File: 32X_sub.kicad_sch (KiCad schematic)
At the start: 98 parts, among them IC511 315-5684, IC512 315-5788, IC515 74HC74, IC516 74LS00, T520 TestPoint, T526 TestPoint, T527 TestPoint, T528 TestPoint, T547 TestPoint, T548 TestPoint, T555 TestPoint, T599 AS, X501 *3

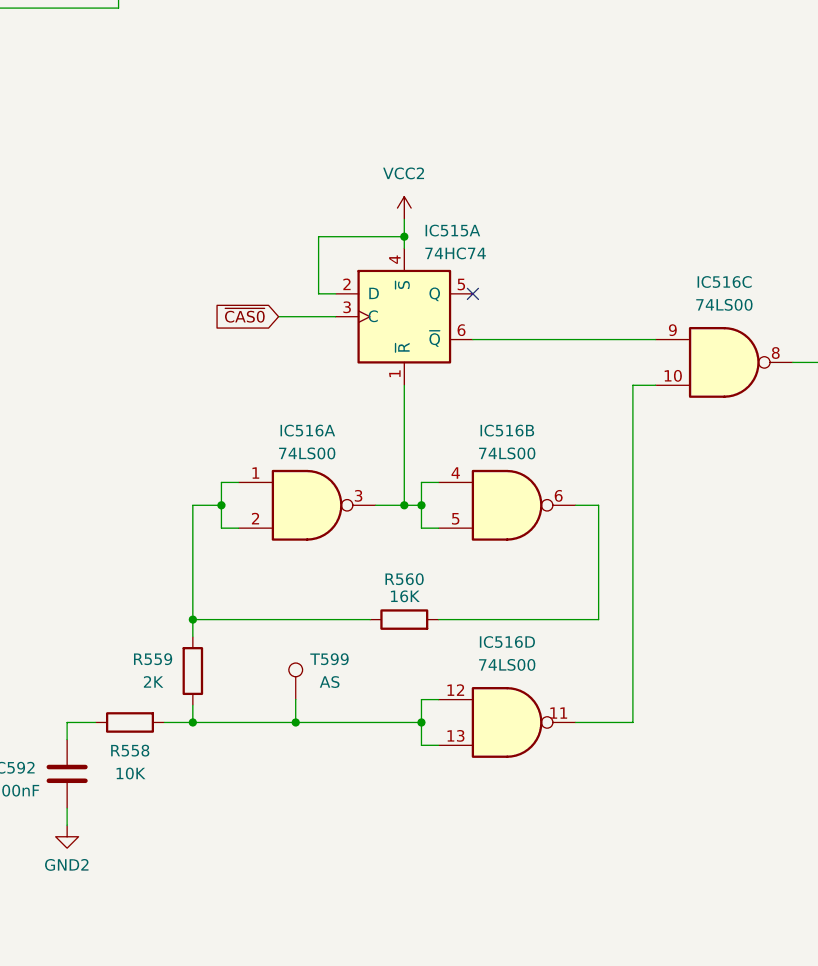
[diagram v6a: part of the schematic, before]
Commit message: Review/add 32X bodges.
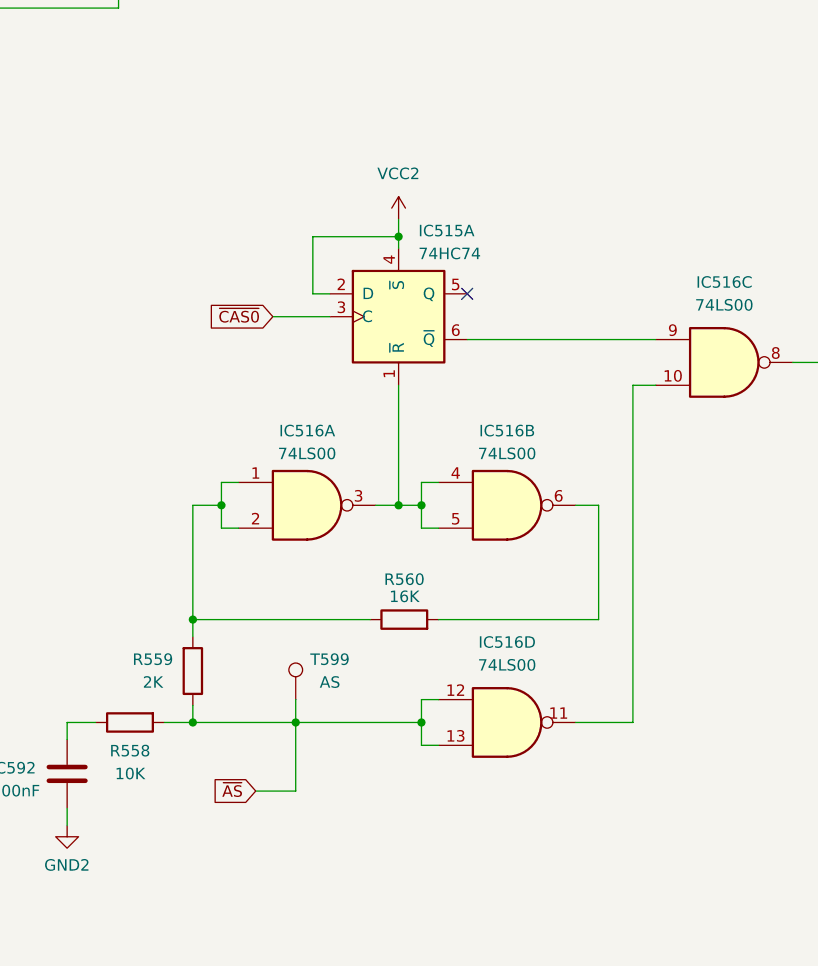
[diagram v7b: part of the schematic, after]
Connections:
- net ~{AS}: now reaches IC516.12, IC516.13, R558.2, R559.1, T599.1
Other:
- moved on the sheet: IC515A
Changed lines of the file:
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@@
   (junction (at 172.085 254.635) (diameter 0) (color 0 0 0 0)
   )
+  (junction (at 183.515 230.505) (diameter 0) (color 0 0 0 0)
+  )
   (junction (at 97.155 129.54) (diameter 0) (color 0 0 0 0)
   )
-  (junction (at 184.15 200.66) (diameter 0) (color 0 0 0 0)
+  (junction (at 183.515 200.66) (diameter 0) (color 0 0 0 0)
   )
   (junction (at 169.545 101.6) (diameter 0) (color 0 0 0 0)
@@
   (junction (at 259.08 116.84) (diameter 0) (color 0 0 0 0)
   )
-  (junction (at 184.15 230.505) (diameter 0) (color 0 0 0 0)
-  )
   (junction (at 91.44 53.34) (diameter 0) (color 0 0 0 0)
   )
@@
   (no_connect (at 134.62 86.36))
   (no_connect (at 134.62 93.98))
-  (no_connect (at 191.77 207.01))
+  (no_connect (at 191.135 207.01))
   (no_connect (at 134.62 88.9))
   (no_connect (at 134.62 91.44))
@@
     (stroke (width 0) (type default))
   )
-  (wire (pts (xy 174.625 207.01) (xy 174.625 200.66))
+  (wire (pts (xy 173.99 207.01) (xy 173.99 200.66))
     (stroke (width 0) (type default))
   )
@@
     (stroke (width 0) (type default))
   )
-  (wire (pts (xy 184.15 230.505) (xy 184.15 217.17))
+  (wire (pts (xy 183.515 230.505) (xy 183.515 217.17))
     (stroke (width 0) (type default))
   )
@@
     (stroke (width 0) (type default))
   )
-  (wire (pts (xy 176.53 207.01) (xy 174.625 207.01))
+  (wire (pts (xy 175.895 207.01) (xy 173.99 207.01))
     (stroke (width 0) (type default))
   )
@@
     (stroke (width 0) (type default))
   )
-  (wire (pts (xy 184.15 198.755) (xy 184.15 200.66))
+  (wire (pts (xy 183.515 198.755) (xy 183.515 200.66))
     (stroke (width 0) (type default))
   )
@@
     (stroke (width 0) (type default))
   )
-  (wire (pts (xy 180.975 230.505) (xy 184.15 230.505))
+  (wire (pts (xy 180.975 230.505) (xy 183.515 230.505))
+    (stroke (width 0) (type default))
+  )
+  (wire (pts (xy 172.085 262.255) (xy 172.085 254.635))
     (stroke (width 0) (type default))
   )
@@
     (stroke (width 0) (type default))
   )
-  (wire (pts (xy 184.15 230.505) (xy 186.055 230.505))
-    (stroke (width 0) (type default))
-  )
   (wire (pts (xy 270.51 38.1) (xy 270.51 44.45))
     (stroke (width 0) (type default))
@@
     (stroke (width 0) (type default))
   )
+  (wire (pts (xy 167.64 262.255) (xy 172.085 262.255))
+    (stroke (width 0) (type default))
+  )
   (wire (pts (xy 240.665 38.1) (xy 252.73 38.1))
     (stroke (width 0) (type default))
@@
     (stroke (width 0) (type default))
   )
+  (wire (pts (xy 183.515 230.505) (xy 186.055 230.505))
+    (stroke (width 0) (type default))
+  )
   (wire (pts (xy 326.39 88.9) (xy 330.835 88.9))
     (stroke (width 0) (type default))
@@
     (stroke (width 0) (type default))
   )
-  (wire (pts (xy 184.15 200.66) (xy 184.15 201.93))
+  (wire (pts (xy 183.515 200.66) (xy 183.515 201.93))
     (stroke (width 0) (type default))
   )
@@
     (stroke (width 0) (type default))
   )
-  (wire (pts (xy 170.18 209.55) (xy 176.53 209.55))
+  (wire (pts (xy 169.545 209.55) (xy 175.895 209.55))
     (stroke (width 0) (type default))
   )
@@
     (stroke (width 0) (type default))
   )
-  (wire (pts (xy 174.625 200.66) (xy 184.15 200.66))
+  (wire (pts (xy 173.99 200.66) (xy 183.515 200.66))
     (stroke (width 0) (type default))
   )
@@
     (stroke (width 0) (type default))
   )
-  (wire (pts (xy 191.77 212.09) (xy 212.09 212.09))
+  (wire (pts (xy 191.135 212.09) (xy 212.09 212.09))
     (stroke (width 0) (type default))
   )
@@
     )
   )
+  (global_label "~{AS}" (shape input) (at 167.64 262.255 180) (fields_autoplaced)
+    (effects (font (size 1.27 1.27)) (justify right))
+    (property "Intersheetrefs" "${INTERSHEET_REFS}" (at 162.3567 262.255 0)
+      (effects (font (size 1.27 1.27)) (justify right) hide)
+    )
+  )
   (global_label "XBOUT" (shape output) (at 367.665 43.18 0) (fields_autoplaced)
     (effects (font (size 1.27 1.27)) (justify left))
@@
     )
   )
-  (global_label "~{CAS0}" (shape input) (at 170.18 209.55 180) (fields_autoplaced)
+  (global_label "~{CAS0}" (shape input) (at 169.545 209.55 180) (fields_autoplaced)
     (effects (font (size 1.27 1.27)) (justify right))
-    (property "Intersheetrefs" "${INTERSHEET_REFS}" (at 162.4172 209.55 0)
+    (property "Intersheetrefs" "${INTERSHEET_REFS}" (at 161.7822 209.55 0)
       (effects (font (size 1.27 1.27)) (justify right) hide)
     )
@@
     )
   )
-  (symbol (lib_id "74xx:74LS74") (at 184.15 209.55 0) (unit 1)
+  (symbol (lib_id "74xx:74LS74") (at 183.515 209.55 0) (unit 1)
     (in_bom yes) (on_board yes) (dnp no) (fields_autoplaced)
-    (property "Reference" "IC515" (at 186.3441 200.025 0)
+    (property "Reference" "IC515" (at 185.7091 200.025 0)
       (effects (font (size 1.27 1.27)) (justify left))
     )
-    (property "Value" "74HC74" (at 186.3441 202.565 0)
+    (property "Value" "74HC74" (at 185.7091 202.565 0)
       (effects (font (size 1.27 1.27)) (justify left))
     )
-    (property "Footprint" "Package_SO:SO-14_3.9x8.65mm_P1.27mm" (at 184.15 209.55 0)
+    (property "Footprint" "Package_SO:SO-14_3.9x8.65mm_P1.27mm" (at 183.515 209.55 0)
       (effects (font (size 1.27 1.27)) hide)
     )
-    (property "Datasheet" "74xx/74hc_hct74.pdf" (at 184.15 209.55 0)
+    (property "Datasheet" "74xx/74hc_hct74.pdf" (at 183.515 209.55 0)
       (effects (font (size 1.27 1.27)) hide)
     )
@@
     )
   )
-  (symbol (lib_id "32X:VCC2") (at 184.15 198.755 0) (unit 1)
+  (symbol (lib_id "32X:VCC2") (at 183.515 198.755 0) (unit 1)
     (in_bom yes) (on_board yes) (dnp no) (fields_autoplaced)
-    (property "Reference" "#PWR0137" (at 184.15 202.565 0)
+    (property "Reference" "#PWR0137" (at 183.515 202.565 0)
       (effects (font (size 1.27 1.27)) hide)
     )
-    (property "Value" "VCC2" (at 184.15 193.675 0)
+    (property "Value" "VCC2" (at 183.515 193.675 0)
       (effects (font (size 1.27 1.27)))
     )
-    (property "Footprint" "" (at 184.15 198.755 0)
+    (property "Footprint" "" (at 183.515 198.755 0)
       (effects (font (size 1.27 1.27)) hide)
     )
-    (property "Datasheet" "" (at 184.15 198.755 0)
+    (property "Datasheet" "" (at 183.515 198.755 0)
       (effects (font (size 1.27 1.27)) hide)
     )

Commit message: Schematic review/fixes.
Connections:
- net VCC2: now also C592.2, R558.1
- net at IC511.30 (HPIN2), R517.1, R518.2: no longer R519.2
- net at C557.1, IC511.6 (MOUT1): now also R519.2
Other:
- moved on the sheet: R519, R520
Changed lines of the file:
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@@
   (junction (at 112.395 250.19) (diameter 0) (color 0 0 0 0)
   )
-  (junction (at 91.44 114.3) (diameter 0) (color 0 0 0 0)
-  )
   (junction (at 270.51 66.04) (diameter 0) (color 0 0 0 0)
   )
   (junction (at 142.875 149.86) (diameter 0) (color 0 0 0 0)
   )
-  (junction (at 97.155 147.32) (diameter 0) (color 0 0 0 0)
-  )
   (junction (at 91.44 47.625) (diameter 0) (color 0 0 0 0)
   )
@@
   (junction (at 328.93 129.54) (diameter 0) (color 0 0 0 0)
   )
+  (junction (at 146.685 254.635) (diameter 0) (color 0 0 0 0)
+  )
   (junction (at 112.395 219.71) (diameter 0) (color 0 0 0 0)
   )
@@
   (junction (at 260.35 71.12) (diameter 0) (color 0 0 0 0)
   )
+  (junction (at 91.44 124.46) (diameter 0) (color 0 0 0 0)
+  )
   (junction (at 328.93 142.24) (diameter 0) (color 0 0 0 0)
   )
@@
   (junction (at 183.515 230.505) (diameter 0) (color 0 0 0 0)
   )
-  (junction (at 97.155 129.54) (diameter 0) (color 0 0 0 0)
-  )
   (junction (at 183.515 200.66) (diameter 0) (color 0 0 0 0)
   )
@@
   (junction (at 186.055 230.505) (diameter 0) (color 0 0 0 0)
   )
-  (junction (at 97.155 138.43) (diameter 0) (color 0 0 0 0)
+  (junction (at 91.44 138.43) (diameter 0) (color 0 0 0 0)
   )
   (junction (at 160.655 243.205) (diameter 0) (color 0 0 0 0)
@@
   (junction (at 252.73 38.1) (diameter 0) (color 0 0 0 0)
   )
+  (junction (at 91.44 147.32) (diameter 0) (color 0 0 0 0)
+  )
   (junction (at 160.655 254.635) (diameter 0) (color 0 0 0 0)
   )
@@
   (junction (at 351.79 99.06) (diameter 0) (color 0 0 0 0)
   )
+  (junction (at 83.82 114.3) (diameter 0) (color 0 0 0 0)
+  )
   (no_connect (at 295.91 116.84))
   (no_connect (at 332.74 226.695))
@@
     (stroke (width 0) (type default))
   )
-  (wire (pts (xy 97.155 138.43) (xy 97.155 139.065))
+  (wire (pts (xy 91.44 138.43) (xy 91.44 139.065))
     (stroke (width 0) (type default))
   )
@@
     (stroke (width 0) (type default))
   )
-  (wire (pts (xy 97.155 147.32) (xy 83.82 147.32))
-    (stroke (width 0) (type default))
-  )
   (wire (pts (xy 53.975 73.66) (xy 64.135 73.66))
     (stroke (width 0) (type default))
@@
     (stroke (width 0) (type default))
   )
-  (wire (pts (xy 83.82 114.3) (xy 91.44 114.3))
-    (stroke (width 0) (type default))
-  )
   (wire (pts (xy 350.52 127) (xy 350.52 128.27))
     (stroke (width 0) (type default))
@@
     (stroke (width 0) (type default))
   )
-  (wire (pts (xy 97.155 138.43) (xy 104.14 138.43))
+  (wire (pts (xy 91.44 138.43) (xy 104.14 138.43))
     (stroke (width 0) (type default))
   )
@@
     (stroke (width 0) (type default))
   )
-  (wire (pts (xy 104.14 129.54) (xy 97.155 129.54))
+  (wire (pts (xy 83.82 129.54) (xy 104.14 129.54))
     (stroke (width 0) (type default))
   )
@@
     (stroke (width 0) (type default))
   )
-  (wire (pts (xy 104.14 114.3) (xy 91.44 114.3))
+  (wire (pts (xy 83.82 114.3) (xy 104.14 114.3))
     (stroke (width 0) (type default))
   )
@@
     (stroke (width 0) (type default))
   )
-  (wire (pts (xy 97.155 129.54) (xy 97.155 130.175))
-    (stroke (width 0) (type default))
-  )
   (wire (pts (xy 152.4 33.02) (xy 152.4 55.88))
     (stroke (width 0) (type default))
@@
     (stroke (width 0) (type default))
   )
+  (wire (pts (xy 91.44 124.46) (xy 104.14 124.46))
+    (stroke (width 0) (type default))
+  )
   (wire (pts (xy 196.215 33.02) (xy 202.565 33.02))
     (stroke (width 0) (type default))
@@
     (stroke (width 0) (type default))
   )
+  (wire (pts (xy 91.44 124.46) (xy 91.44 130.175))
+    (stroke (width 0) (type default))
+  )
   (wire (pts (xy 240.665 71.12) (xy 248.92 71.12))
     (stroke (width 0) (type default))
@@
     (stroke (width 0) (type default))
   )
-  (wire (pts (xy 91.44 109.22) (xy 93.345 109.22))
+  (wire (pts (xy 83.82 109.22) (xy 93.345 109.22))
+    (stroke (width 0) (type default))
+  )
+  (wire (pts (xy 146.685 251.46) (xy 146.685 254.635))
     (stroke (width 0) (type default))
   )
@@
     (stroke (width 0) (type default))
   )
+  (wire (pts (xy 91.44 147.32) (xy 83.82 147.32))
+    (stroke (width 0) (type default))
+  )
   (wire (pts (xy 340.995 127) (xy 347.98 127))
     (stroke (width 0) (type default))
@@
     (stroke (width 0) (type default))
   )
-  (wire (pts (xy 97.155 137.795) (xy 97.155 138.43))
+  (wire (pts (xy 91.44 137.795) (xy 91.44 138.43))
     (stroke (width 0) (type default))
   )
@@
     (stroke (width 0) (type default))
   )
-  (wire (pts (xy 97.155 129.54) (xy 83.82 129.54))
-    (stroke (width 0) (type default))
-  )
   (bus (pts (xy 85.09 255.27) (xy 85.09 252.73))
     (stroke (width 0) (type default))
@@
     (stroke (width 0) (type default))
   )
-  (wire (pts (xy 104.14 147.32) (xy 97.155 147.32))
+  (wire (pts (xy 91.44 147.32) (xy 104.14 147.32))
     (stroke (width 0) (type default))
   )
@@
     (stroke (width 0) (type default))
   )
-  (wire (pts (xy 97.155 146.685) (xy 97.155 147.32))
+  (wire (pts (xy 91.44 146.685) (xy 91.44 147.32))
     (stroke (width 0) (type default))
   )
@@
     (stroke (width 0) (type default))
   )
-  (wire (pts (xy 91.44 114.3) (xy 91.44 109.22))
-    (stroke (width 0) (type default))
-  )
-  (wire (pts (xy 104.14 124.46) (xy 91.44 124.46))
+  (wire (pts (xy 83.82 114.3) (xy 83.82 109.22))
     (stroke (width 0) (type default))
   )
@@
     )
   )
-  (symbol (lib_id "Device:R") (at 97.155 142.875 180) (unit 1)
+  (symbol (lib_id "Device:R") (at 91.44 142.875 180) (unit 1)
     (in_bom yes) (on_board yes) (dnp no)
-    (property "Reference" "R520" (at 101.6 142.24 0)
+    (property "Reference" "R520" (at 95.885 142.24 0)
       (effects (font (size 1.27 1.27)))
     )
-    (property "Value" "10K" (at 101.6 144.145 0)
+    (property "Value" "10K" (at 95.885 144.145 0)
       (effects (font (size 1.27 1.27)))
     )
-    (property "Footprint" "Resistor_SMD:R_0805_2012Metric" (at 98.933 142.875 90)
+    (property "Footprint" "Resistor_SMD:R_0805_2012Metric" (at 93.218 142.875 90)
       (effects (font (size 1.27 1.27)) hide)
     )
-    (property "Datasheet" "~" (at 97.155 142.875 0)
+    (property "Datasheet" "~" (at 91.44 142.875 0)
       (effects (font (size 1.27 1.27)) hide)
     )
@@
     )
   )
+  (symbol (lib_id "32X:VCC2") (at 146.685 251.46 0) (unit 1)
+    (in_bom yes) (on_board yes) (dnp no) (fields_autoplaced)
+    (property "Reference" "#PWR0185" (at 146.685 255.27 0)
+      (effects (font (size 1.27 1.27)) hide)
+    )
+    (property "Value" "VCC2" (at 146.685 246.38 0)
+      (effects (font (size 1.27 1.27)))
+    )
+    (property "Footprint" "" (at 146.685 251.46 0)
+      (effects (font (size 1.27 1.27)) hide)
+    )
+    (property "Datasheet" "" (at 146.685 251.46 0)
+      (effects (font (size 1.27 1.27)) hide)
+    )
+    (pin "1")
+    (instances
+      (project "Neptune"
+        (path "/bcc23b51-b742-4ae5-9dd6-d96a24058944/edde10e2-ce08-4180-9fbe-ab298dfbfa4c"
+          (reference "#PWR0185") (unit 1)
+        )
+      )
+    )
+  )
   (symbol (lib_id "Device:C_Variable") (at 264.795 93.98 270) (mirror x) (unit 1)
     (in_bom yes) (on_board yes) (dnp no)
@@
     )
   )
-  (symbol (lib_id "Device:R") (at 97.155 133.985 180) (unit 1)
+  (symbol (lib_id "Device:R") (at 91.44 133.985 180) (unit 1)
     (in_bom yes) (on_board yes) (dnp no)
-    (property "Reference" "R519" (at 101.6 133.35 0)
+    (property "Reference" "R519" (at 95.885 133.35 0)
       (effects (font (size 1.27 1.27)))
     )
-    (property "Value" "8.2K" (at 101.6 135.255 0)
+    (property "Value" "8.2K" (at 95.885 135.255 0)
       (effects (font (size 1.27 1.27)))
     )
-    (property "Footprint" "Resistor_SMD:R_0805_2012Metric" (at 98.933 133.985 90)
+    (property "Footprint" "Resistor_SMD:R_0805_2012Metric" (at 93.218 133.985 90)
       (effects (font (size 1.27 1.27)) hide)
     )
-    (property "Datasheet" "~" (at 97.155 133.985 0)
+    (property "Datasheet" "~" (at 91.44 133.985 0)
       (effects (font (size 1.27 1.27)) hide)
     )
